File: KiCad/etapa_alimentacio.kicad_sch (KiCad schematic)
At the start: 12 parts, among them J4 Conn_01x02_Pin, U1 LM2596S-12, U2 LM1117DT-3.3

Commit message: ALFRED DEGANOS SECOOOOS PLS DADDY ALFRED TE CAMELAMOS
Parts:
- added TP1: Tp_3.3V, TestPoint:TestPoint_Keystone_5015_Micro_Mini, symbol Connector:TestPoint
- added TP2: Tp_5V, TestPoint:TestPoint_Keystone_5015_Micro_Mini, symbol Connector:TestPoint
- added TP3: Tp_12V, TestPoint:TestPoint_Keystone_5015_Micro_Mini, symbol Connector:TestPoint
- added TP6: Tp_GND, TestPoint:TestPoint_Keystone_5015_Micro_Mini, symbol Connector:TestPoint
- added TP7: Tp_GNDPWR, TestPoint:TestPoint_Keystone_5015_Micro_Mini, symbol Connector:TestPoint
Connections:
- net +12V: now also TP3.1
- net +3.3V: now also TP1.1
- net GND: now also TP6.1
- net GNDPWR: now also TP7.1
- net at Cin_reg1.1, Cout_DCDC1.1, L_DCDC1.2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: now also TP2.1

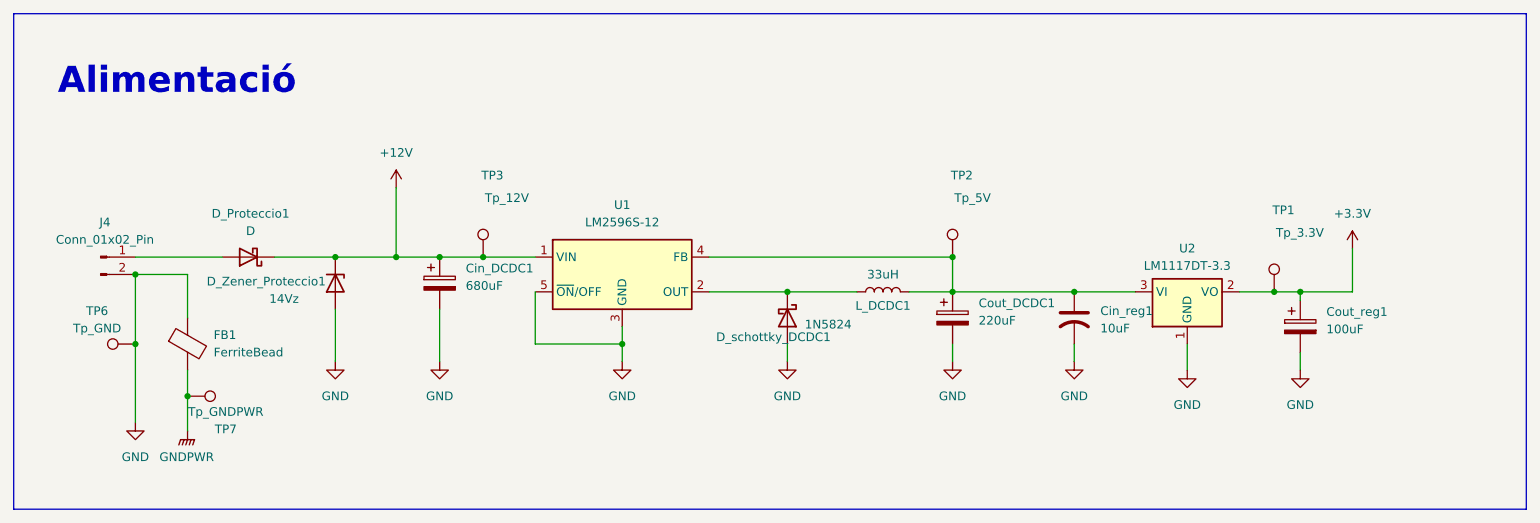
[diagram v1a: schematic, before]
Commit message: Routing de l'alimentació fet, s'ha afegit connector del mòdul RF i plànols millorats
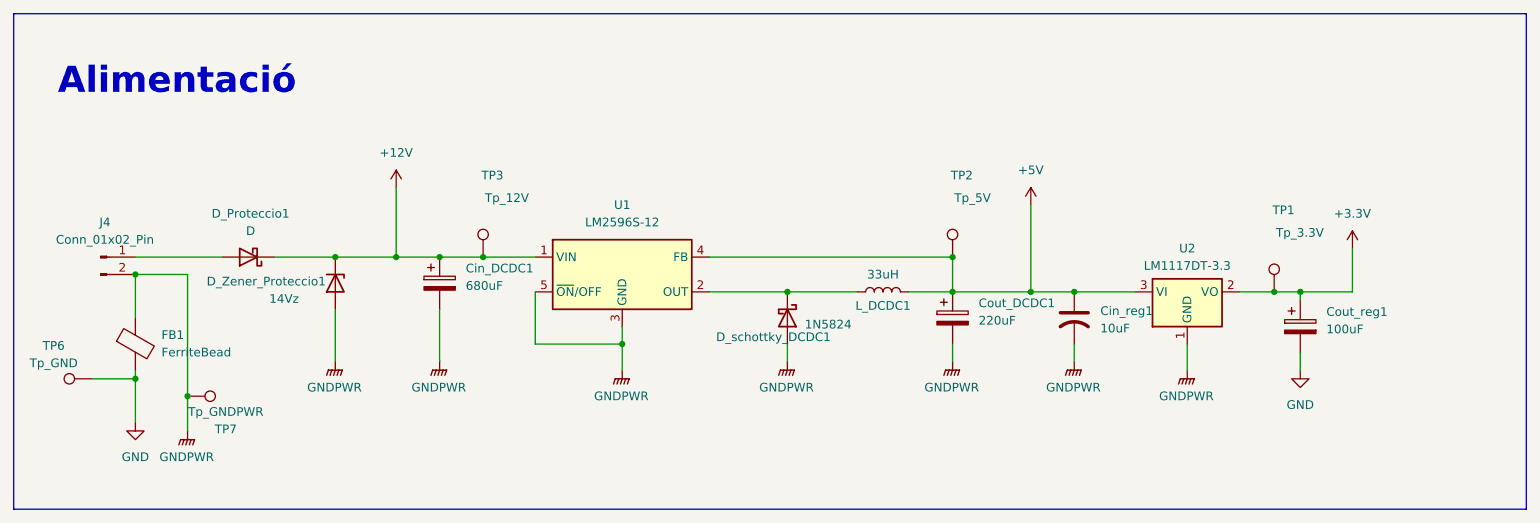
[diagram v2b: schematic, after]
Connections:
- net GND: now also FB1.2; no longer Cin_DCDC1.2, Cin_reg1.2, Cout_DCDC1.2, D_Zener_Proteccio1.2 (A), D_schottky_DCDC1.2 (A), FB1.1, J4.2 (Pin_2), U1.3 (GND), U1.5 (~{ON}/OFF), U2.1 (GND)
- net GNDPWR: now also Cin_DCDC1.2, Cin_reg1.2, Cout_DCDC1.2, D_Zener_Proteccio1.2 (A), D_schottky_DCDC1.2 (A), FB1.1, J4.2 (Pin_2), U1.3 (GND), U1.5 (~{ON}/OFF), U2.1 (GND); no longer FB1.2
- net +5V: now reaches Cin_reg1.1, Cout_DCDC1.1, L_DCDC1.2, TP2.1, U1.4 (FB), U2.3 (VI)
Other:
- moved on the sheet: FB1, TP6
